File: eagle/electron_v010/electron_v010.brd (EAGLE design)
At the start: 20.3 x 50.8 mm, 91 parts, among them J1 SIM-NANO-4FF, J2 IPEX-20279-001E, U1 U-BLOX-SARA-U260, U2 SN74AVC4T245, U3 STM32F205RG, U4 MAX1704X, U5 SN74LVC1G07, U6 SN74LVC1G07, U8 SN74AVC4T245, X1 USB-MICROB, Y1 32Khz, Y2 26Mhz

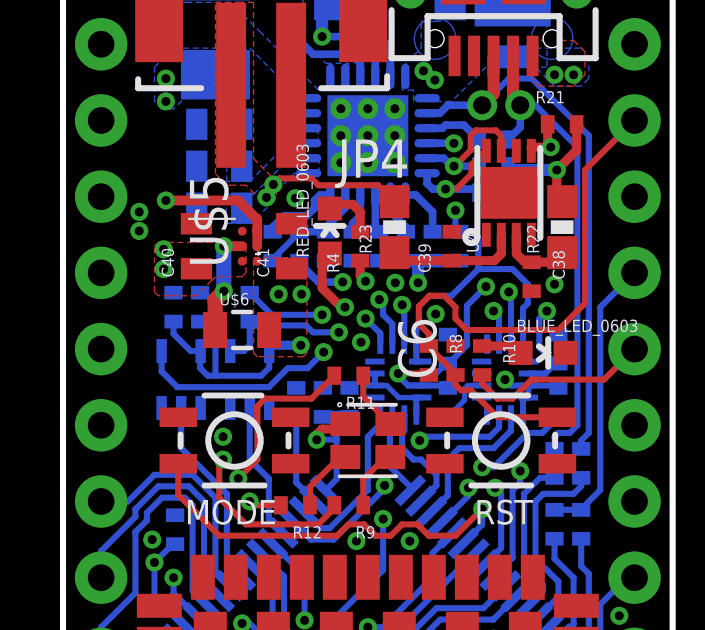
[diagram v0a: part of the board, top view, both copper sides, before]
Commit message: #8 Updated 3.3V regulator's inductor package footprint
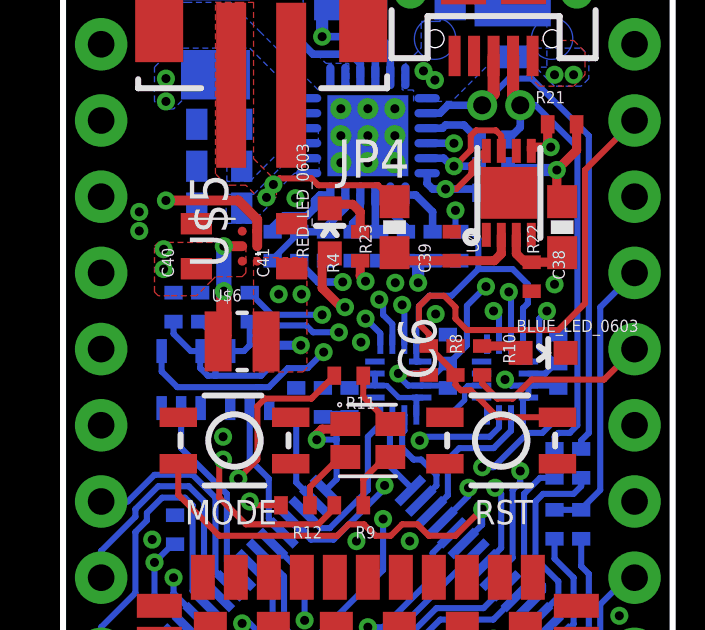
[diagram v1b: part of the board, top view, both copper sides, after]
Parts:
- U$6: device SparkFun-Passives:0805 -> Particle:INDUCTOR-0805
- moved U$6 0.38 mm to (5.97, 37.1)
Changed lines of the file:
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@@
 <element name="R19" library="Spark" package="R0402_B" value="10K" x="8.763" y="40.259" locked="yes" rot="MR270"/>
 <element name="C7" library="Spark" package="C0402_B" value="47nF" x="7.747" y="48.514" locked="yes" rot="MR90"/>
-<element name="U$6" library="SparkFun-Passives" package="0805" value="0.47uH" x="5.969" y="37.465" locked="yes"/>
+<element name="U$6" library="Particle" package="INDUCTOR-0805" value="0.47uH" x="5.969" y="37.084" locked="yes"/>
 <element name="C40" library="Bretts-Spark-Library" package="C0603_B" value="2.2uF" x="4.445" y="40.259" locked="yes" rot="R90"/>
 <element name="C41" library="Bretts-Spark-Library" package="C0603_B" value="2.2uF" x="7.62" y="40.259" locked="yes" rot="R90"/>
@@
 <vertex x="8.001" y="39.878"/>
 <vertex x="8.128" y="39.751"/>
-<vertex x="8.128" y="36.703"/>
-<vertex x="8.001" y="36.576"/>
-<vertex x="6.477" y="36.576"/>
-<vertex x="6.35" y="36.703"/>
+<vertex x="8.128" y="36.195"/>
+<vertex x="8.001" y="36.068"/>
+<vertex x="6.35" y="36.068"/>
 </polygon>
 <wire x1="6.604" y1="35.941" x2="6.873" y2="36.21" width="0.2032" layer="16"/>
@@
 <wire x1="5.3594" y1="40.259" x2="5.3594" y2="38.7604" width="0.508" layer="16"/>
 <wire x1="5.973" y1="40.259" x2="5.3594" y2="40.259" width="0.3302" layer="1"/>
-<wire x1="5.3594" y1="38.7604" x2="5.069" y2="38.47" width="0.508" layer="1"/>
-<wire x1="5.069" y1="38.47" x2="5.069" y2="37.465" width="0.508" layer="1"/>
+<wire x1="5.3594" y1="38.7604" x2="5.3594" y2="37.2744" width="0.508" layer="1"/>
+<wire x1="5.3594" y1="37.2744" x2="5.169" y2="37.084" width="0.508" layer="1"/>
 </signal>
 <signal name="N$2">
